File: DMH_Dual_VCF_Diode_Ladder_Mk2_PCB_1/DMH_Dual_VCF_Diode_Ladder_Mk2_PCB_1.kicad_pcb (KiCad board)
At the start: 2 copper layers, 146 x 175 mm, 223 parts, among them J0 Conn_01x01, J1 TS_Jack_6.35mm_Sw, J10 TS_Jack_6.35mm_Sw, J100 IDC_02x08, J11 TS_Jack_6.35mm_Sw, J12 TS_Jack_6.35mm_Sw, J13 TS_Jack_6.35mm_Sw, J14 TS_Jack_6.35mm_Sw, J15 Conn_01x08_PinHeader, J16 Conn_01x08_PinHeader, J17 Conn_01x06_PinHeader, J18 Conn_01x06_PinHeader, J19 Conn_01x06_PinHeader, J2 TS_Jack_6.35mm_Sw, J20 Conn_01x06_PinHeader, J200 IDC_02x05, J21 Conn_01x06_PinHeader, J210 IDC_02x05, J22 Conn_01x06_PinHeader, J23 Conn_01x04_PinHeader, J3 TS_Jack_6.35mm_Sw, J4 TS_Jack_6.35mm_Sw, J5 TS_Jack_6.35mm_Sw, J6 TS_Jack_6.35mm_Sw, J7 TS_Jack_6.35mm_Sw, J8 TS_Jack_6.35mm_Sw, J9 TS_Jack_6.35mm_Sw, Q1 BC548, Q2 BC548, Q3 BC548, Q4 BC548, Q5 BC548, Q6 BC548, Q7 BC548, Q8 BC548, U1 TL074, U10 TL074, U2 TL074, U3 TL074, U4 TL074, U5 TL074, U6 TL074, U7 TL074, U8 TL074, U9 TL074

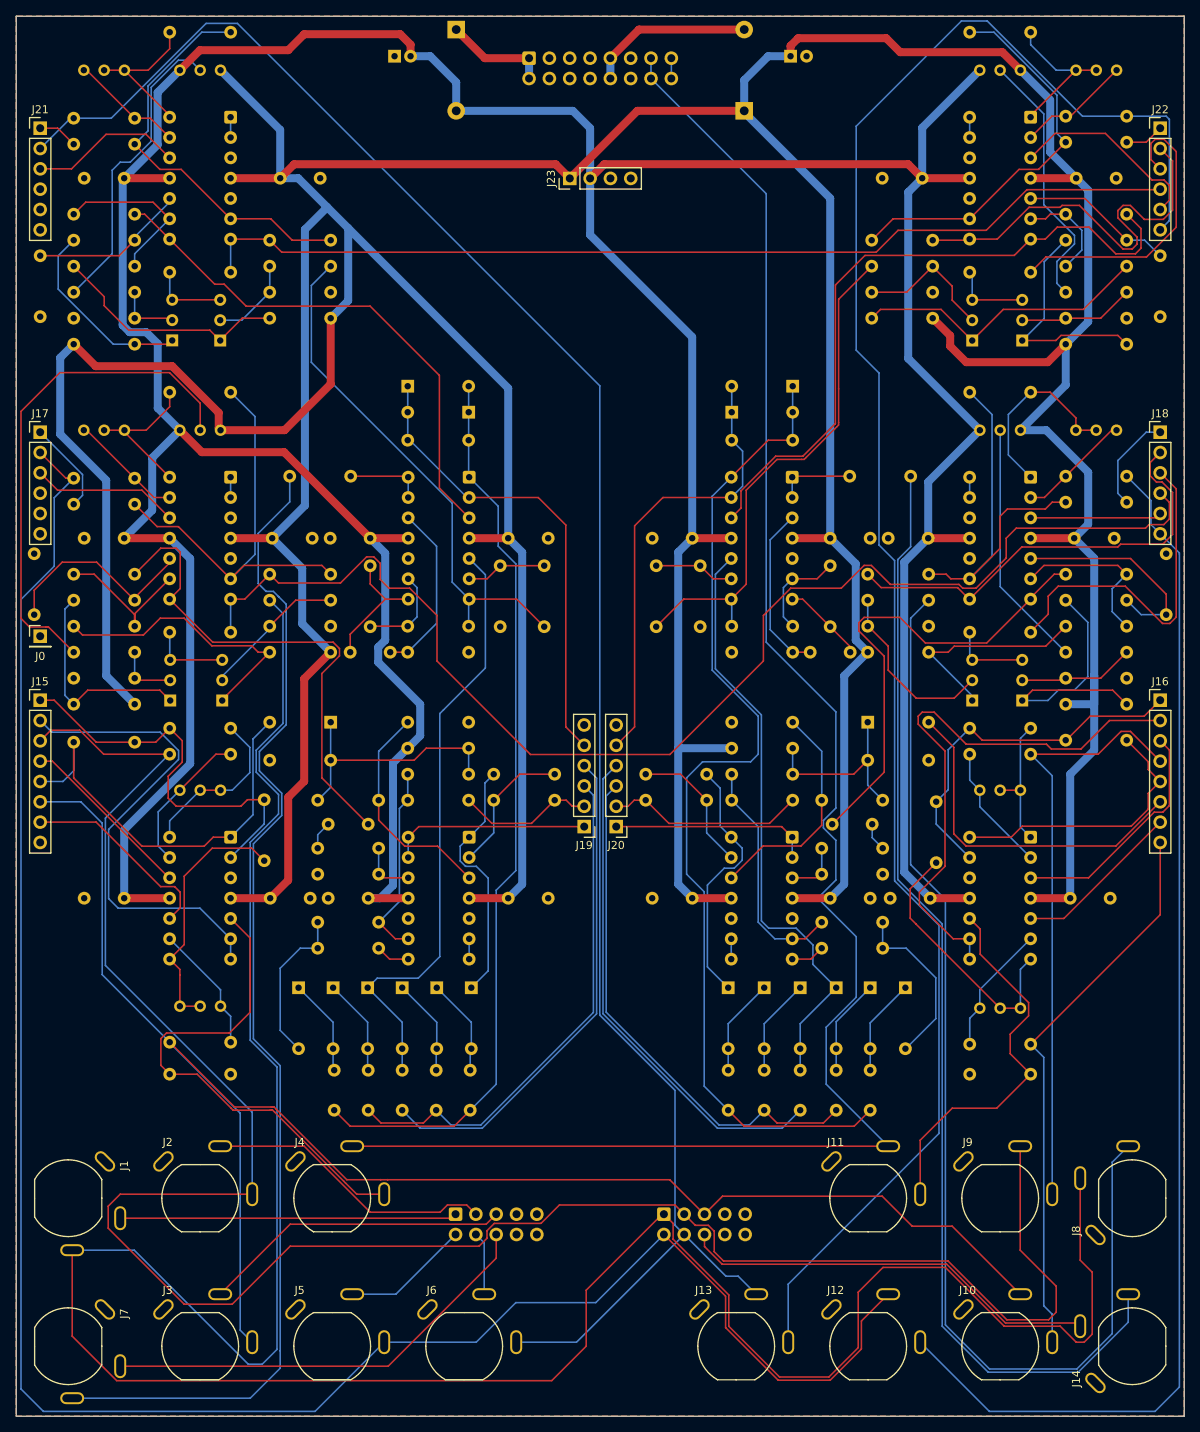
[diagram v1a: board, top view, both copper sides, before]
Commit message: KiCad 9.0.7 + centralized library
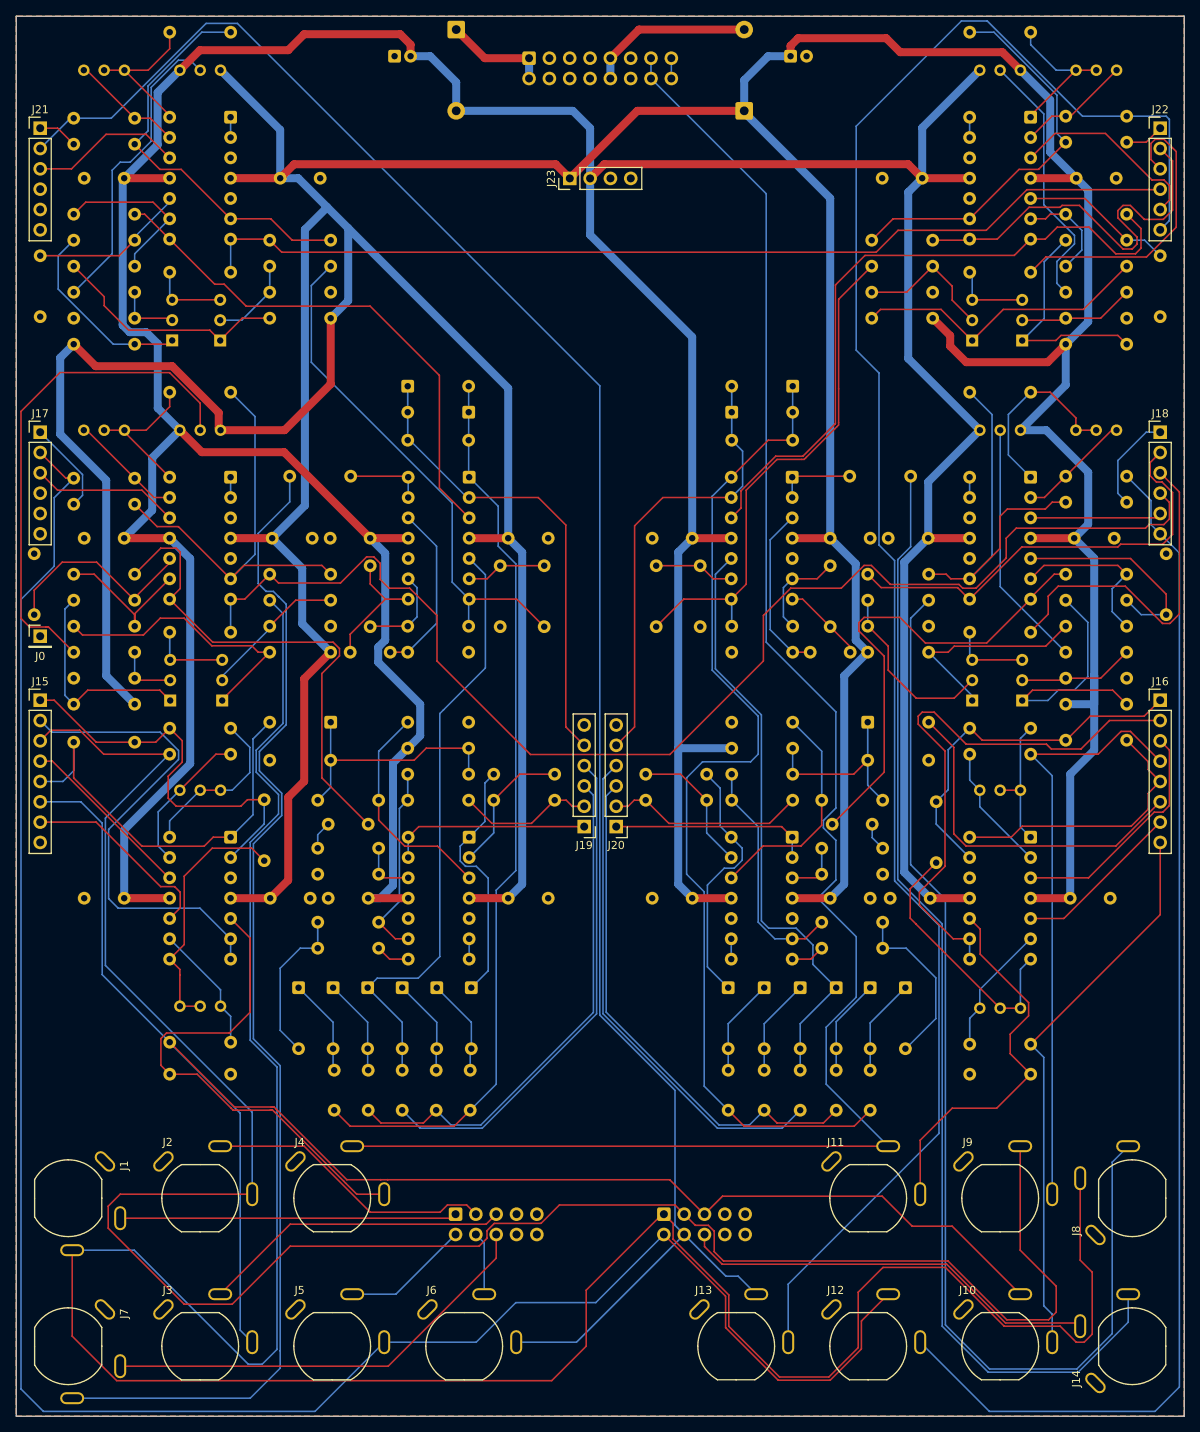
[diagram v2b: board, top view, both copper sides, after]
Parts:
- D1: value SB140+ -> SB140
- D2: value SB140- -> SB140
